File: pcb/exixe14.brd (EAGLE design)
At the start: 20 x 40 mm, 51 parts

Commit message: refining board design for production run
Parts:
- removed R17: 10K, joyAnalog:0805
- renumbered U$2 to IC1
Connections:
- net +3V3: no longer R17.2
- net NRST: no longer R17.1
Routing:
- net +3V3: track 73.1 -> 70.2 mm
- net +180V: track 20.1 -> 19.1 mm

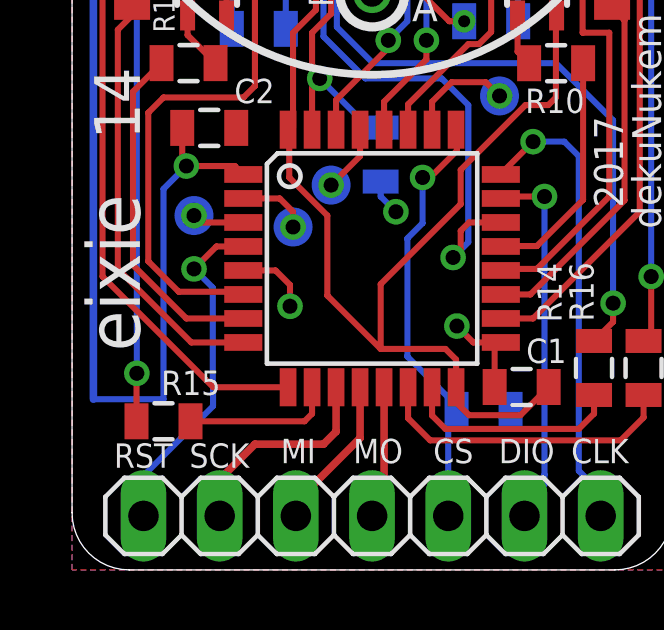
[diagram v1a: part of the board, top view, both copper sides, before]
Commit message: adjusted passive values
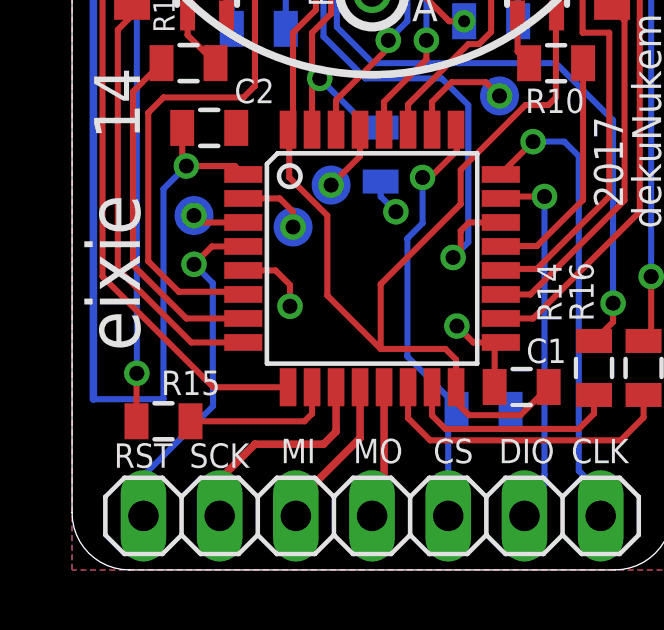
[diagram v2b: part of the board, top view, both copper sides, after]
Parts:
- R20, R21, R25: value 68K -> 10K
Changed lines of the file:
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@@
 <attribute name="VALUE" x="9.144" y="12.192" size="0.0254" layer="28" rot="MR0"/>
 </element>
-<element name="R20" library="joyAnalog" package="0805" value="68K" x="13.97" y="18.288" smashed="yes" rot="MR180">
+<element name="R20" library="joyAnalog" package="0805" value="10K" x="13.97" y="18.288" smashed="yes" rot="MR180">
 <attribute name="NAME" x="15.494" y="18.6309" size="0.8128" layer="26" rot="MR180"/>
 </element>
-<element name="R21" library="joyAnalog" package="0805" value="68K" x="6.223" y="18.034" smashed="yes" rot="MR180">
+<element name="R21" library="joyAnalog" package="0805" value="10K" x="6.223" y="18.034" smashed="yes" rot="MR180">
 <attribute name="NAME" x="5.461" y="17.2085" size="0.8128" layer="26" rot="MR180"/>
 </element>
-<element name="R25" library="joyAnalog" package="0805" value="68K" x="10.287" y="13.843" smashed="yes" rot="MR90">
+<element name="R25" library="joyAnalog" package="0805" value="10K" x="10.287" y="13.843" smashed="yes" rot="MR90">
 <attribute name="NAME" x="11.9634" y="15.5829" size="0.8128" layer="26" rot="MR0"/>
 </element>
@@
 <contactref element="IC1" pad="4"/>
 <contactref element="JP2" pad="1"/>
-<via x="4.064" y="10.033" extent="1-16" drill="0.5"/>
-<wire x1="5.7074" y1="10.781" x2="4.812" y2="10.781" width="0.2032" layer="1"/>
-<wire x1="4.812" y1="10.781" x2="4.064" y2="10.033" width="0.2032" layer="1"/>
-<wire x1="4.064" y1="10.033" x2="4.688" y2="9.409" width="0.2032" layer="16"/>
+<via x="4.064" y="10.1854" extent="1-16" drill="0.5"/>
 <wire x1="2.38" y1="1.8" x2="2.38" y2="3.142" width="0.2032" layer="16"/>
 <wire x1="2.38" y1="3.142" x2="4.699" y2="5.461" width="0.2032" layer="16"/>
 <wire x1="4.699" y1="6.212" x2="4.699" y2="5.461" width="0.2032" layer="16"/>
-<wire x1="4.688" y1="9.409" x2="4.688" y2="6.223" width="0.2032" layer="16"/>
-<wire x1="4.688" y1="6.223" x2="4.699" y2="6.212" width="0.2032" layer="16"/>
+<wire x1="4.699" y1="6.212" x2="4.688" y2="6.223" width="0.2032" layer="16"/>
+<wire x1="4.6596" y1="10.781" x2="4.064" y2="10.1854" width="0.2032" layer="1"/>
+<wire x1="5.7074" y1="10.781" x2="4.6596" y2="10.781" width="0.2032" layer="1"/>
+<wire x1="4.688" y1="9.5614" x2="4.064" y2="10.1854" width="0.2032" layer="16"/>
+<wire x1="4.688" y1="6.223" x2="4.688" y2="9.5614" width="0.2032" layer="16"/>
 </signal>
 <signal name="UART_TX">

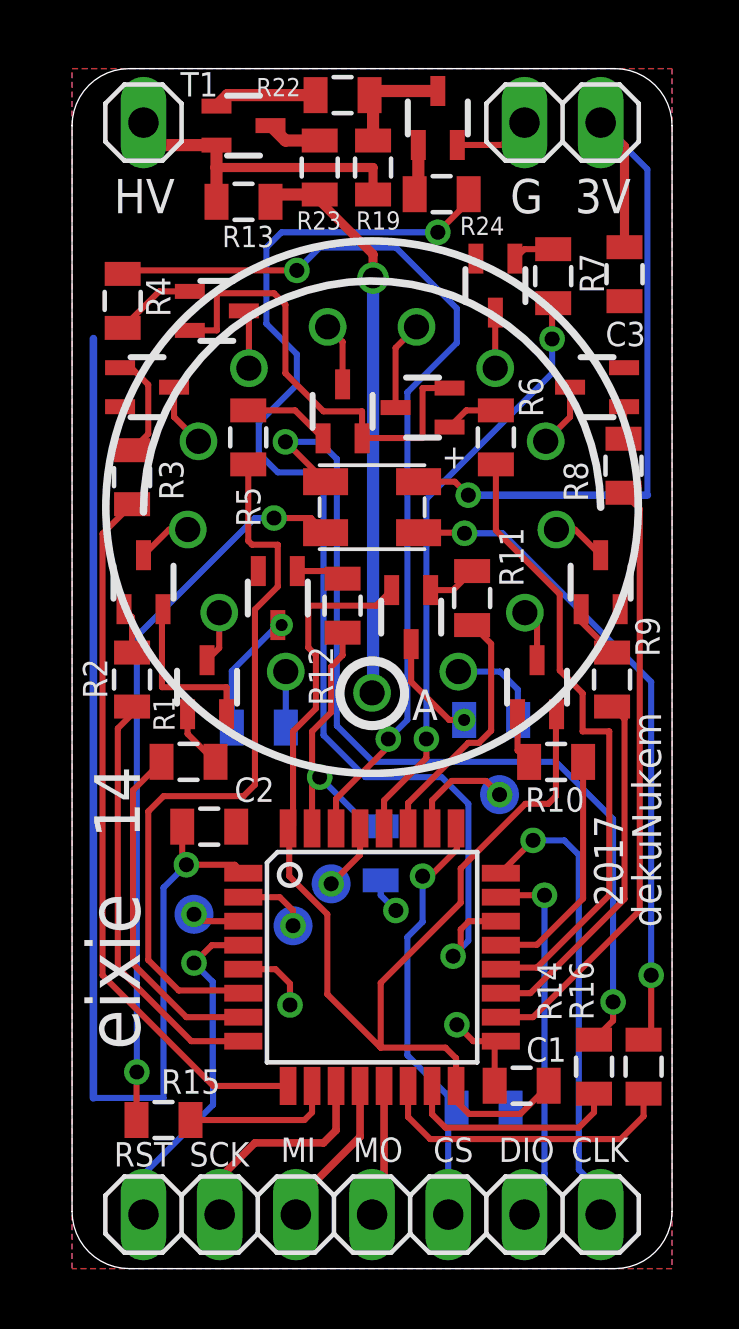
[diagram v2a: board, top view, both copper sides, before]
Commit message: changed testpoints to unpopulated resistors
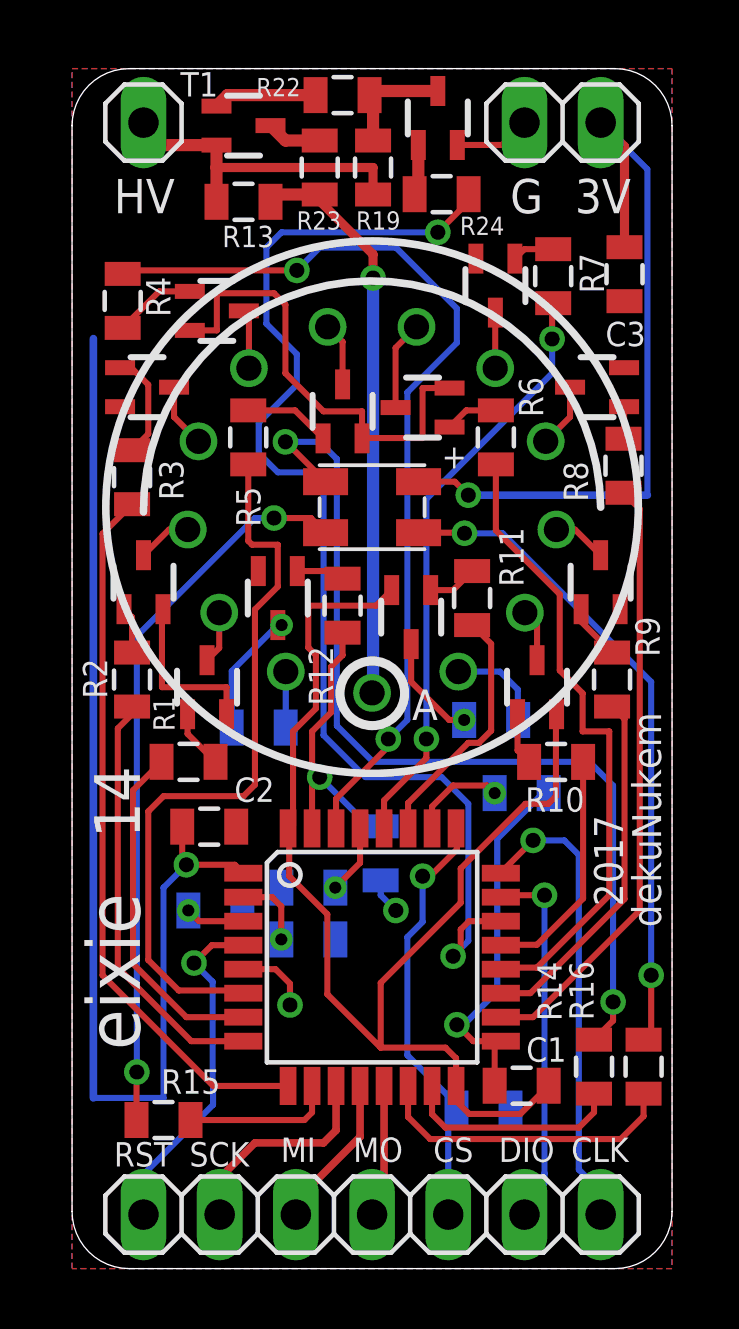
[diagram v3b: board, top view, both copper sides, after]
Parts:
- removed TP1, TP2, TP3, TP4: PTR1TP13R, testpad:TP13R
- added R17, R26, R27, R28: 10K, joyAnalog:0805
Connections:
- net +3V3: now also R17.2, R26.2, R27.1, R28.1
- net N$16: now also R26.1; no longer TP2.TP
- net N$2: now also R17.1; no longer TP1.TP
- net N$25: now also R27.2; no longer TP4.TP
- net UART_TX: now also R28.2; no longer TP3.TP
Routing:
- net +3V3: track 70.2 -> 79.4 mm
- net N$15: track 30.8 -> 31.5 mm
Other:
- board text removed: "PB3"
- board text removed: "PF0"
- board text removed: "PF1"
- board text removed: "TX"

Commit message: adjusted values
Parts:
- C1: value 1uF -> 100nF
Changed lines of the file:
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@@
 <attribute name="NAME" x="2.7071" y="19.0796" size="0.7112" layer="25" font="vector" rot="R270"/>
 </element>
-<element name="C1" library="joyAnalog" package="0805" value="1uF" x="14.986" y="6.096" smashed="yes">
+<element name="C1" library="joyAnalog" package="0805" value="100nF" x="14.986" y="6.096" smashed="yes">
 <attribute name="NAME" x="15.1384" y="6.8961" size="0.8128" layer="25" font="vector"/>
 </element>
